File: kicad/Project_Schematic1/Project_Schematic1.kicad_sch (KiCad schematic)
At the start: 46 parts, among them M1 Flag_Servo, M2 Motor_Left, M3 Motor_Bottom, M4 Motor_Right, Q1 NPN, Q2 NPN, Q3 NPN, U1 74xxx244, U10 MCP6294, U11 MCP6294, U12 SW_CapTouch, U2 PIC32MX170F256B, U3 CD4052, U4 QTR-HD-01A, U5 Left_Drum_LEDs, U6 Bottom_Drum_LEDs, U7 Right_Drum_LEDs, U8 Clock_LEDs, U9 MCP6294

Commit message: Revert to 3d98758
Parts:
- removed C10, C11, C12, C6, C7: 0.1uF, symbol ME218_BaseLib:Cap
- removed C4, C5, C8, C9: 10uF, symbol ME218_BaseLib:Cap
- removed D4, D5, D6: Diode, symbol ME218_BaseLib:Diode
- removed R14, R17: 5K1, symbol ME218_BaseLib:Res1
- removed R15, R6, R8: 3K3, symbol ME218_BaseLib:Res1
- removed R16, R7: Piezo1, symbol ME218_BaseLib:Res_Adj2
- removed U10, U11, U9: MCP6294, symbol ME218_BaseLib:MCP6294
- removed U12: SW_CapTouch, symbol ME218_BaseLib:SW_CapTouch
- removed U8: Clock_LEDs, symbol ME218_BaseLib:Dot_Star
- added C?: .1uF, symbol ME218_BaseLib:Cap
- added C? (x3): 10uF, symbol ME218_BaseLib:Cap
- added D? (x4): FRD, symbol ME218_BaseLib:Diode
- added R10, R11, R12: Res1, symbol ME218_BaseLib:Res1
- added R2, R4, R5: 3.3k, symbol ME218_BaseLib:Res1
- added R? (x3): Piezo1, symbol ME218_BaseLib:Res_Adj2
- added R?: 1k, symbol ME218_BaseLib:Res1
- added R? (x2): 2M, symbol ME218_BaseLib:Res1
- C1, C2, C3: value 0.1uF -> 0.1 uF
- M2: value Motor_Left -> Motor1
- M3: value Motor_Bottom -> Motor2
- M4: value Motor_Right -> Motor2
- R?: renamed from R13; value 5K1 -> 2M
- U5: value Left_Drum_LEDs -> Drum_LEDs
- U6: value Bottom_Drum_LEDs -> Timer_LEDs
- U7: value Right_Drum_LEDs -> Intensity_LEDs
- renumbered R9 to R?
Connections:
- net SCK Clock_LEDs is gone; now on net SCK Timer_LEDs: U3. (sel1)
- net piezo_left_in (AN) is gone; now on net piezo1_in (AN): U2.6 (RB2)
- net +3.3V: now also D1.1 (K), D2.1 (K), D3.1 (K), M2.1 (+), M3.1 (+), M4.1 (+)
- net +5V: no longer D1.1 (K), D2.1 (K), D3.1 (K), M2.1 (+), M3.1 (+), M4.1 (+)
- net 5V SCK: now also U1.3 (2Y0); no longer U1.16 (1Y1)
- net 5V data: now also U1.5 (2Y1); no longer U1.18 (1Y0)
- net GND: now also C?.2, C?.2, C?.2, C?.2, D?.2 (A), D?.2 (A), D?.2 (A), D?.2 (A), R2.2, R4.2, R5.2, R?.1, R?.1, R?.1, R?.2, R?.2, R?.2
- net PIC32 sel0: now also U2.10 (RA3); no longer U2.9 (RA2)
- net PIC32 sel1: now also U2.12 (RA4); no longer U2.18 (PGED2/5VT/RB9)
- net SCK: now also U1.17 (2A0); no longer U1.4 (1A1)
- net SPI data: now also U1.15 (2A1), U2.24 (RB13); no longer U1.2 (1A0), U2.10 (RA3)
- net piezo1_in (AN): now reaches R?.1, R?.2
- net piezo1_in (AN): now also C?.1, D?.1 (K)
- net Motor1: now reaches U2.15 (PGEC3/5VT/RB6)
- net Motor1: now also R10.1
- net Motor2: now reaches U2.16 (5VT/RB7)
- net Motor2: now also R11.1
- net at U4.3 (Signal): now also U2.26 (RB15); no longer U2.24 (RB13)
- net at U2.3 (RA1): now also M1.1 (PWM)
- net 5V Servo_PWM: no longer names the net of U1.14 (1Y2)
- net 5V Servo_PWM: no longer M1.1 (PWM)
- net Cap_Touch: no longer names the net of U2.14 (PGED3/5VT/RB5)
- net Motor_Bottom: no longer names the net of U2.21 (PGEC2/5VT/RB10)
- net Motor_Bottom: no longer Q2.1 (B)
- net Motor_Left: no longer names the net of Q1.1 (B)
- net Motor_Left: now also R10.2; no longer U2.26 (RB15)
- net Motor_Right: no longer names the net of U2.22 (RB11)
- net Motor_Right: no longer Q3.1 (B)
- net PWM to audio PIC renamed Motor3
- net Motor3: now also R12.1
- net SCK Bottom_Drum_LEDs renamed SCK Timer_LEDs
- net SCK Timer_LEDs: now also R4.1
- net SCK Left_Drum_LEDs renamed SCK Drum_LEDs
- net SCK Drum_LEDs: now also R2.1
- net SCK Right_Drum_LEDs renamed SCK Intensity_LEDs
- net SCK Intensity_LEDs: now also R5.1
- net Servo_PWM: no longer names the net of U1.6 (1A2)
- net Servo_PWM: no longer U2.11 (RB4)
- net piezo_bottom_in (AN) renamed piezo2_in (AN)
- net piezo2_in (AN): now also C?.1, D?.1 (K), R?.1, R?.2
- net piezo_right_in (AN): no longer names the net of U2.23 (RB12)
- new net: C?.1, D?.1 (K), R?.1, R?.2
- new net: Q3.1 (B), R12.2
- new net: Q2.1 (B), R11.2
- new net PWM to other PIC: U2.9 (RA2)
- new net piezo3_in (AN): C?.1, D?.1 (K), R?.1, R?.2, U2.11 (RB4)
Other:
- moved on the sheet: C1, C2, C3, D1, D2, D3, M1, M2, M3, M4, Q1, Q2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

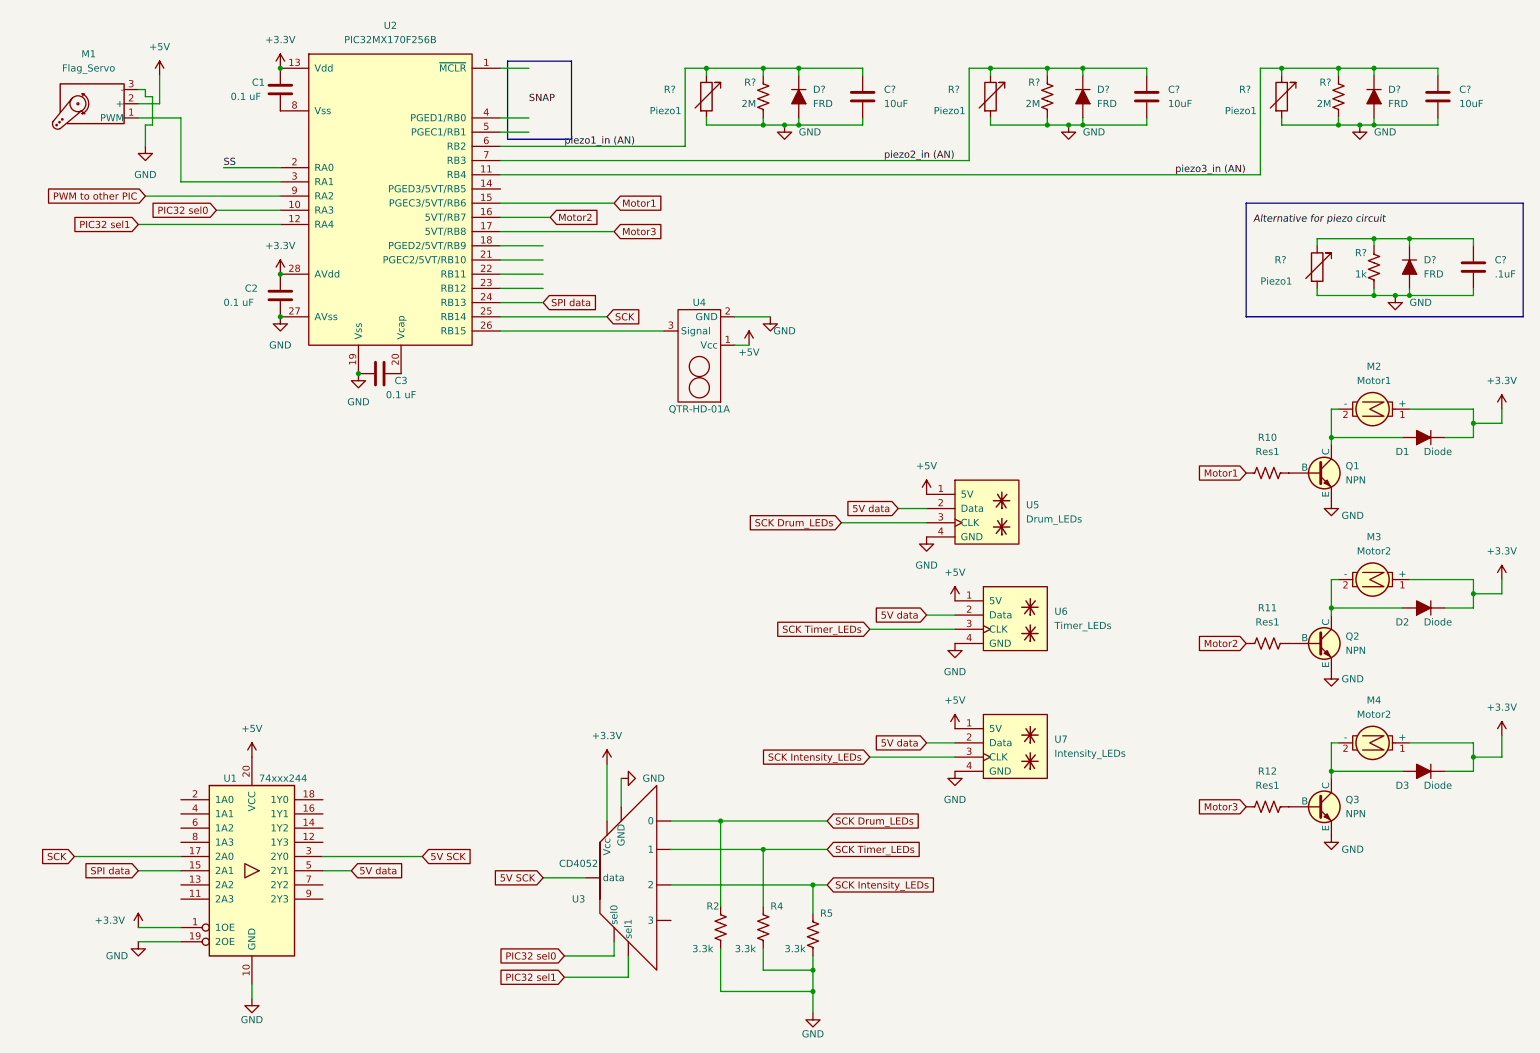
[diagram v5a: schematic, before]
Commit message: Use parallel diode with voltage reference to make up for -600mV diode forward voltage
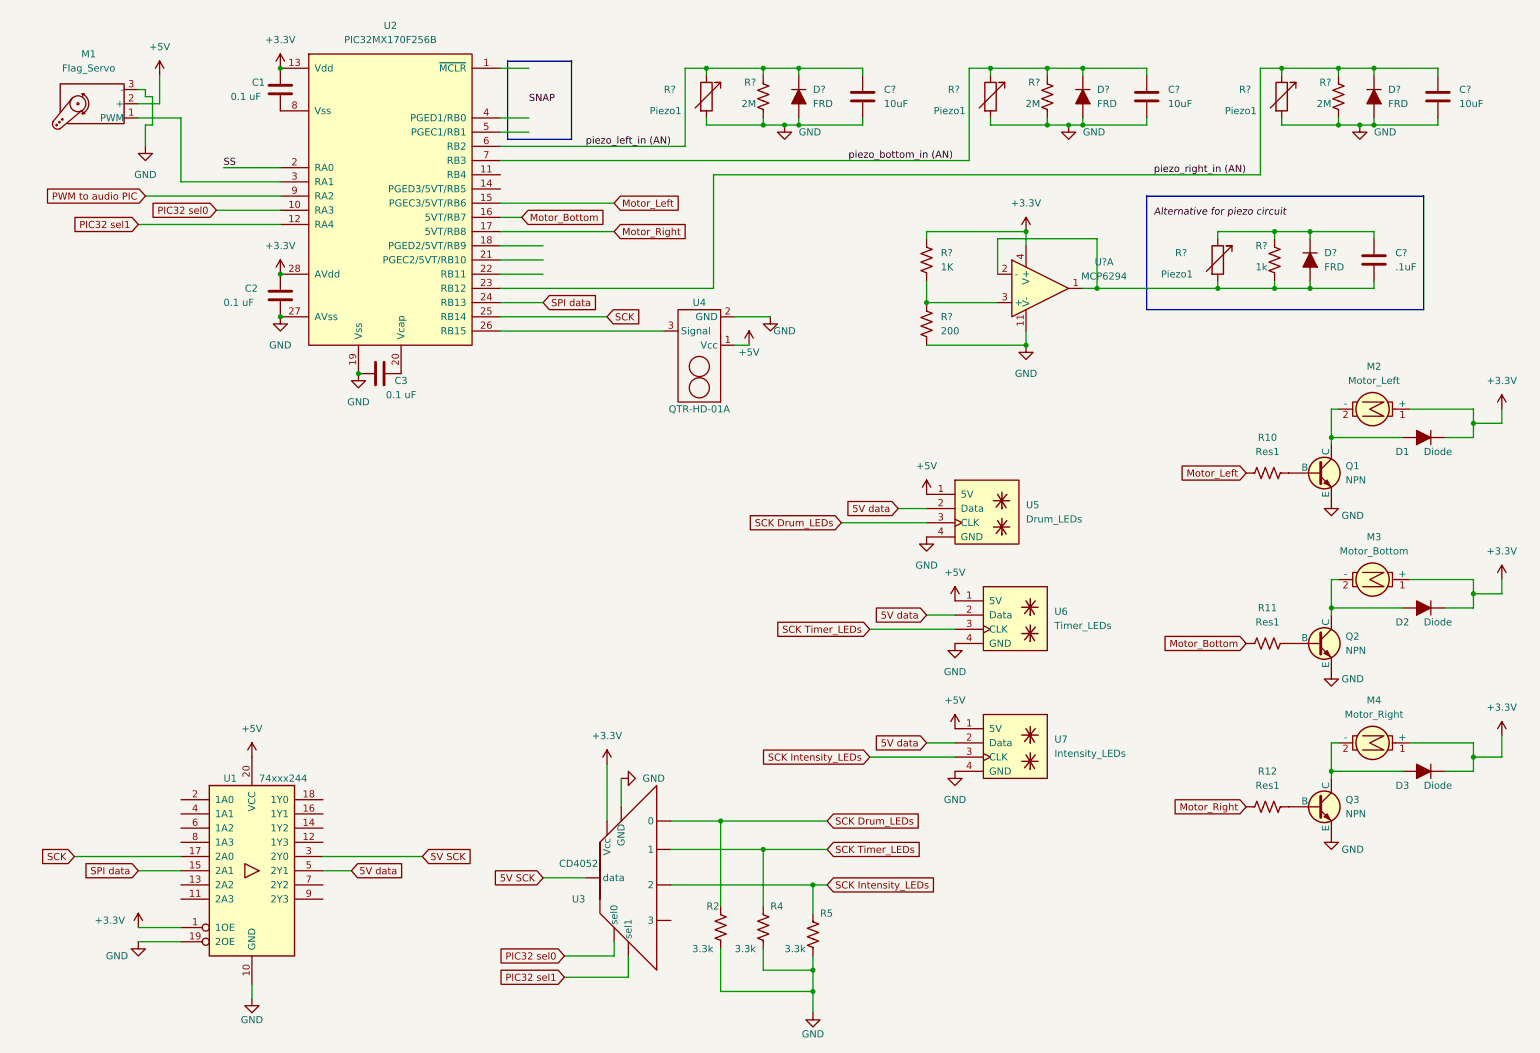
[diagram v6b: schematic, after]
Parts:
- added R?: 1K, symbol ME218_BaseLib:Res1
- added R?: 200, symbol ME218_BaseLib:Res1
- added U?: MCP6294, symbol ME218_BaseLib:MCP6294
- M2: value Motor1 -> Motor_Left
- M3: value Motor2 -> Motor_Bottom
- M4: value Motor2 -> Motor_Right
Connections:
- net +3.3V: now also R?.1, U?.4 (V+)
- net GND: now also R?.2, U?.11 (V-); no longer C?.2, D?.2 (A), R?.1, R?.2
- net piezo_right_in (AN): now reaches U2.23 (RB12)
- net piezo_right_in (AN): now also C?.1, D?.1 (K), R?.1, R?.2
- net Motor1 renamed Motor_Left
- net Motor2 renamed Motor_Bottom
- net Motor3 renamed Motor_Right
- net PWM to other PIC renamed PWM to audio PIC
- net piezo1_in (AN) renamed piezo_left_in (AN)
- net piezo2_in (AN) renamed piezo_bottom_in (AN)
- removed net piezo3_in (AN): C?.1, D?.1 (K), R?.1, R?.2, U2.11 (RB4)
- new net: C?.2, D?.2 (A), R?.1, R?.2, U?.1, U?.2 (-)
- new net: R?.1, R?.2, U?.3 (+)
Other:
- moved on the sheet: C?, D?, R?

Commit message: Redo piezo circuit with diode in serial to pin
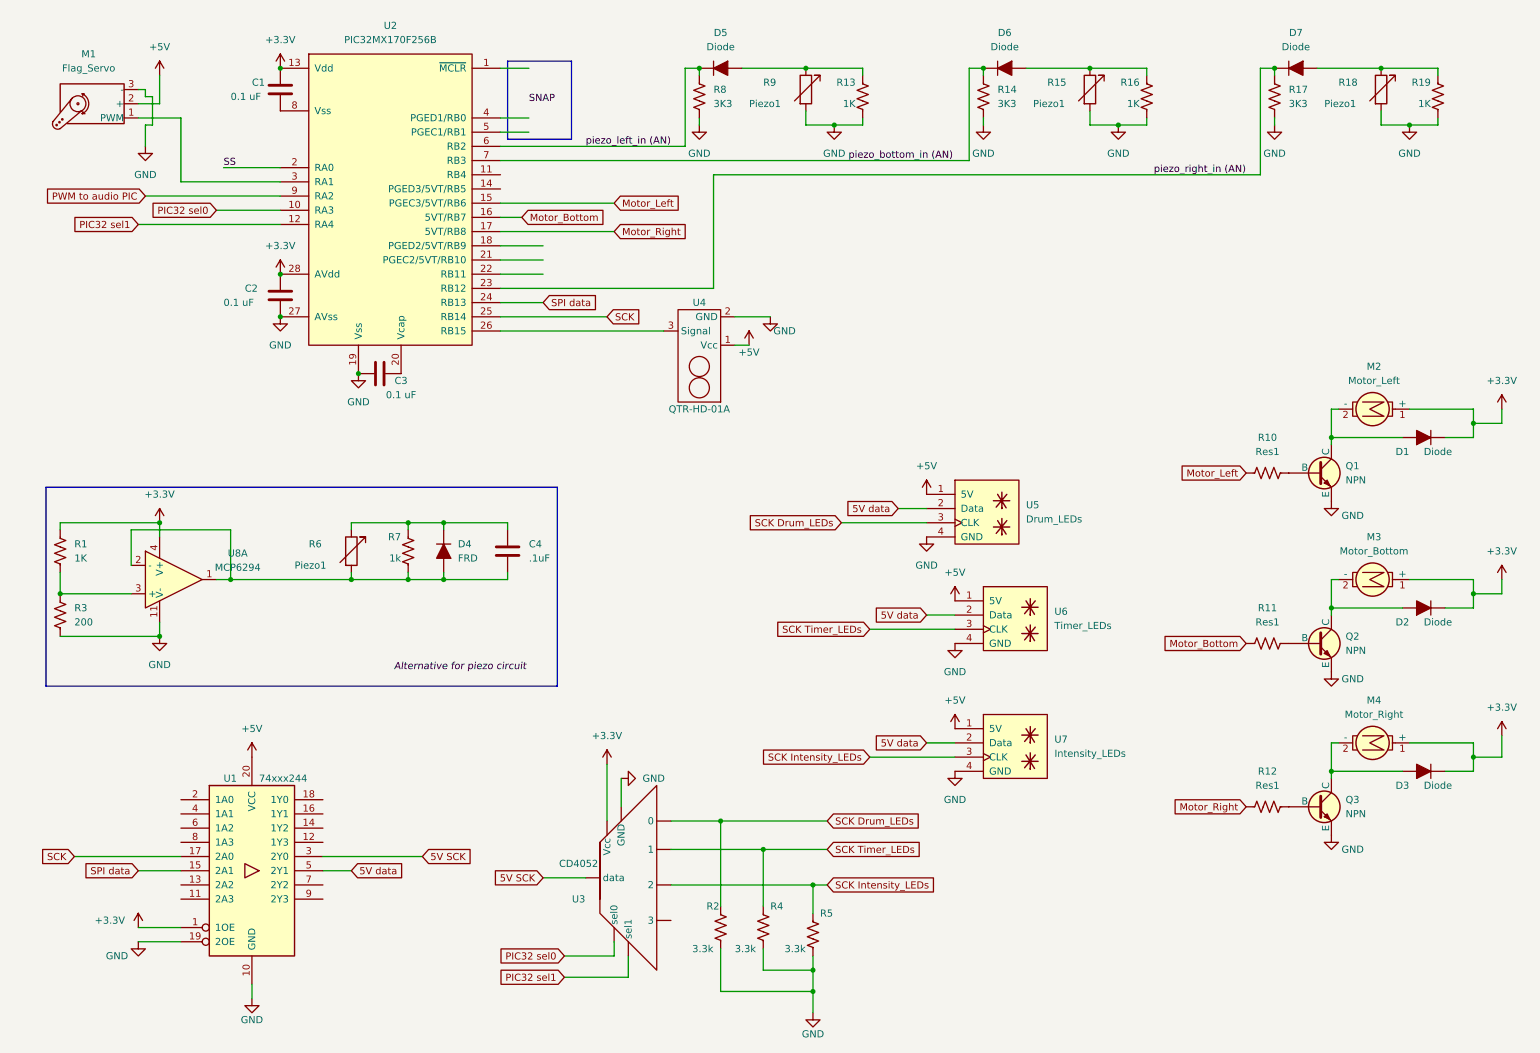
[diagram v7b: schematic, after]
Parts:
- removed C? (x3): 10uF, symbol ME218_BaseLib:Cap
- removed D? (x3): FRD, symbol ME218_BaseLib:Diode
- removed R? (x2): 2M, symbol ME218_BaseLib:Res1
- removed R? (x2): Piezo1, symbol ME218_BaseLib:Res_Adj2
- added D5, D6, D7: Diode, symbol ME218_BaseLib:Diode
- added R14, R17, R8: 3K3, symbol ME218_BaseLib:Res1
- added R15, R18: Piezo1, symbol ME218_BaseLib:Res_Adj2
- added R16, R19: 1K, symbol ME218_BaseLib:Res1
- R13: renamed from R?; value 2M -> 1K
- gave numbers to parts that had none: 8
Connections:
- net GND: now also R14.2, R15.2, R16.1, R17.2, R18.2, R19.1, R8.2
- net piezo_bottom_in (AN): now also D6.1 (K), R14.1
- net piezo_left_in (AN): now also D5.1 (K), R8.1; no longer R13.2, R9.1
- net piezo_right_in (AN): now also D7.1 (K), R17.1
- new net: D5.2 (A), R13.2, R9.1
- new net: D6.2 (A), R15.1, R16.2
- new net: D7.2 (A), R18.1, R19.2
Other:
- moved on the sheet: C4, D4, R1, R13, R3, R6, R7, R9, U8A

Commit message: MUX to each drum LED strip and clock + Remove intensity strip
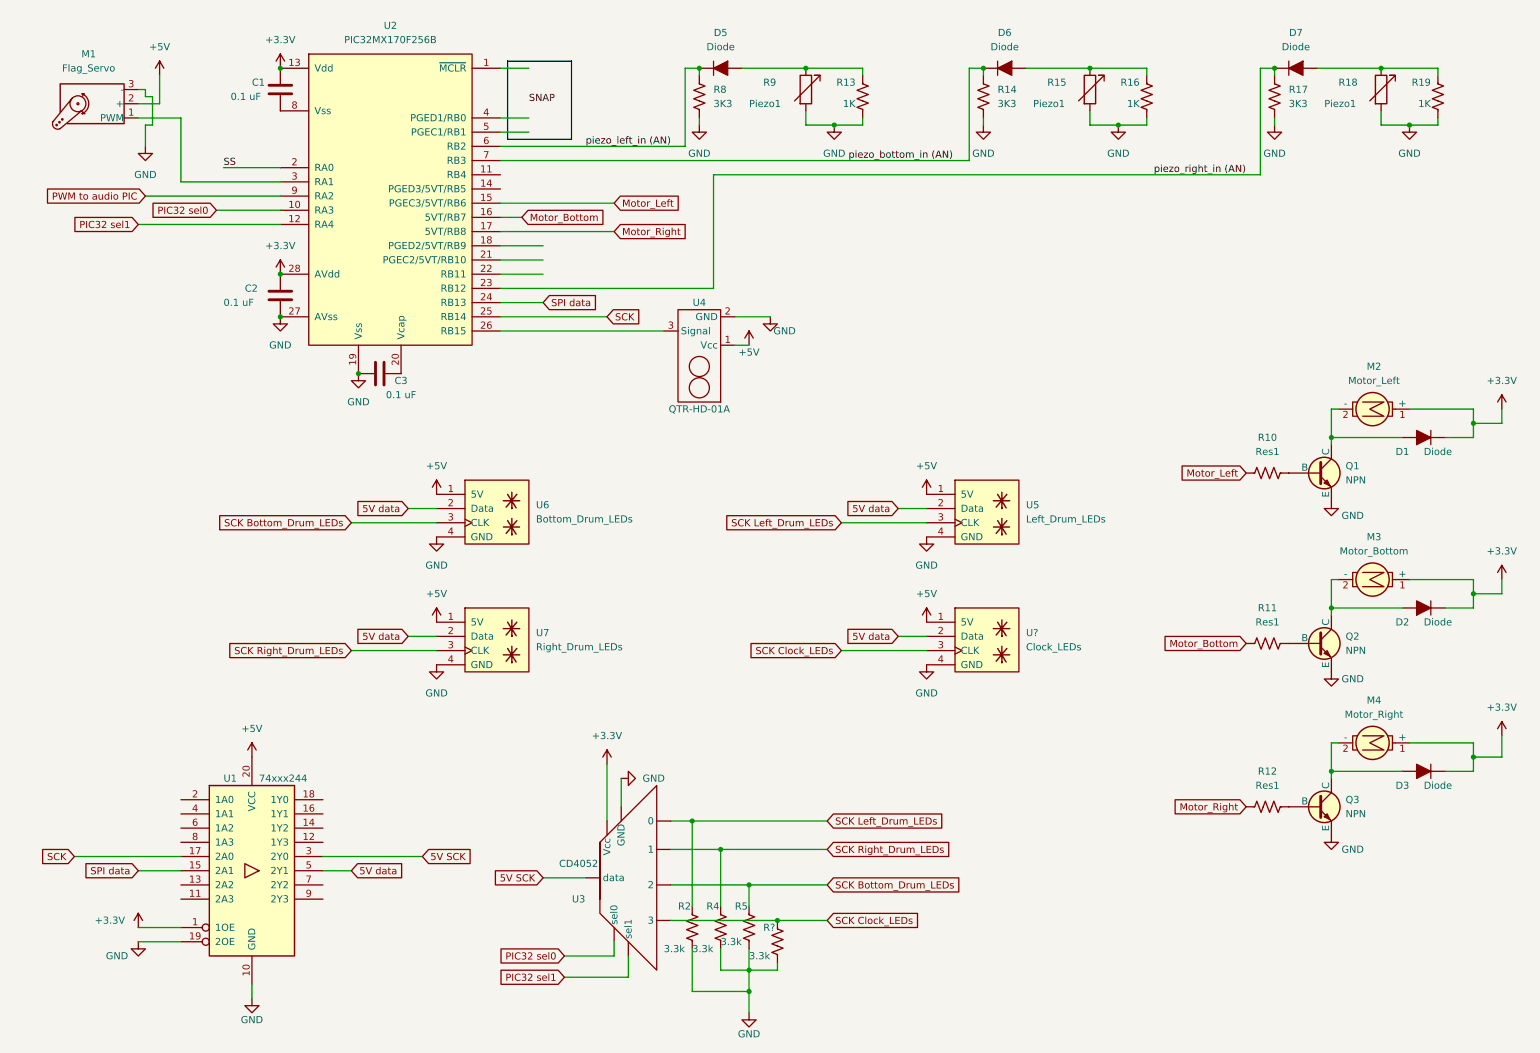
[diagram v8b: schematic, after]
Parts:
- removed C4: .1uF, symbol ME218_BaseLib:Cap
- removed D4: FRD, symbol ME218_BaseLib:Diode
- removed R1: 1K, symbol ME218_BaseLib:Res1
- removed R3: 200, symbol ME218_BaseLib:Res1
- removed R6: Piezo1, symbol ME218_BaseLib:Res_Adj2
- removed R7: 1k, symbol ME218_BaseLib:Res1
- removed U8: MCP6294, symbol ME218_BaseLib:MCP6294
- added R?: 3.3k, symbol ME218_BaseLib:Res1
- added U?: Clock_LEDs, symbol ME218_BaseLib:Dot_Star
- U5: value Drum_LEDs -> Left_Drum_LEDs
- U6: value Timer_LEDs -> Bottom_Drum_LEDs
- U7: value Intensity_LEDs -> Right_Drum_LEDs
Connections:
- net +5V: now also U?.1 (5V)
- net 5V data: now also U?.2 (Data)
- net GND: now also R?.2, U?.4 (GND)
- net SCK Right_Drum_LEDs: now reaches U3. (Vcc)
- net SCK Right_Drum_LEDs: now also R4.1, U7.3 (CLK)
- net SCK Drum_LEDs renamed SCK Left_Drum_LEDs
- removed net SCK Intensity_LEDs: R5.1, U3. (sel1), U7.3 (CLK)
- removed net SCK Timer_LEDs: R4.1, U3. (sel1), U6.3 (CLK)
- new net SCK Bottom_Drum_LEDs: R5.1, U3. (Vcc), U6.3 (CLK)
- new net SCK Clock_LEDs: R?.1, U3. (Vcc), U?.3 (CLK)
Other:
- moved on the sheet: R2, R4, R5, U6, U7
